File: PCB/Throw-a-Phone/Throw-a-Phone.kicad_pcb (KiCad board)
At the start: 2 copper layers, 50 x 87.5 mm, 26 parts, among them J3 Conn_01x04_Pin, SW1 SW_Push, SW10 SW_Push, SW11 SW_Push, SW12 SW_Push, SW2 SW_Push, SW3 SW_Push, SW4 SW_Push, SW5 SW_Push, SW6 SW_Push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

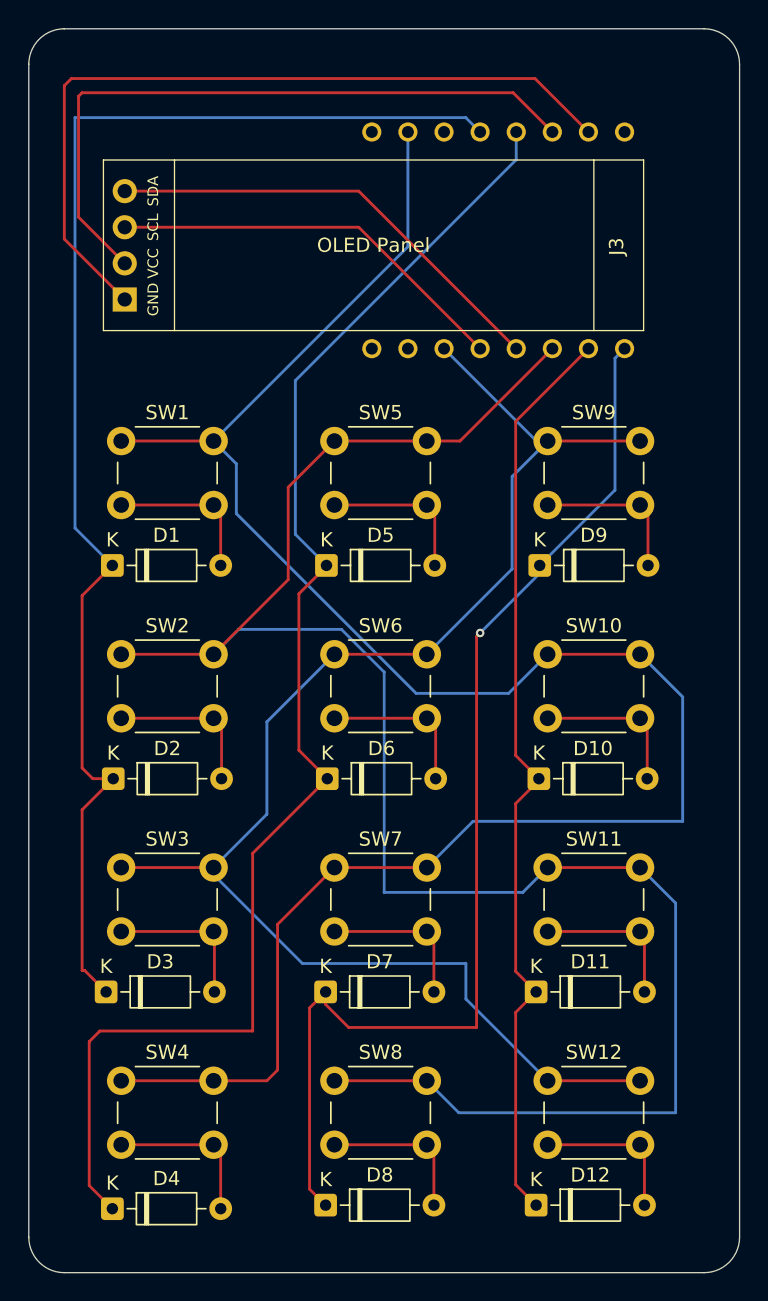
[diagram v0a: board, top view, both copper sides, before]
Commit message: Made enclosure, edited PCB
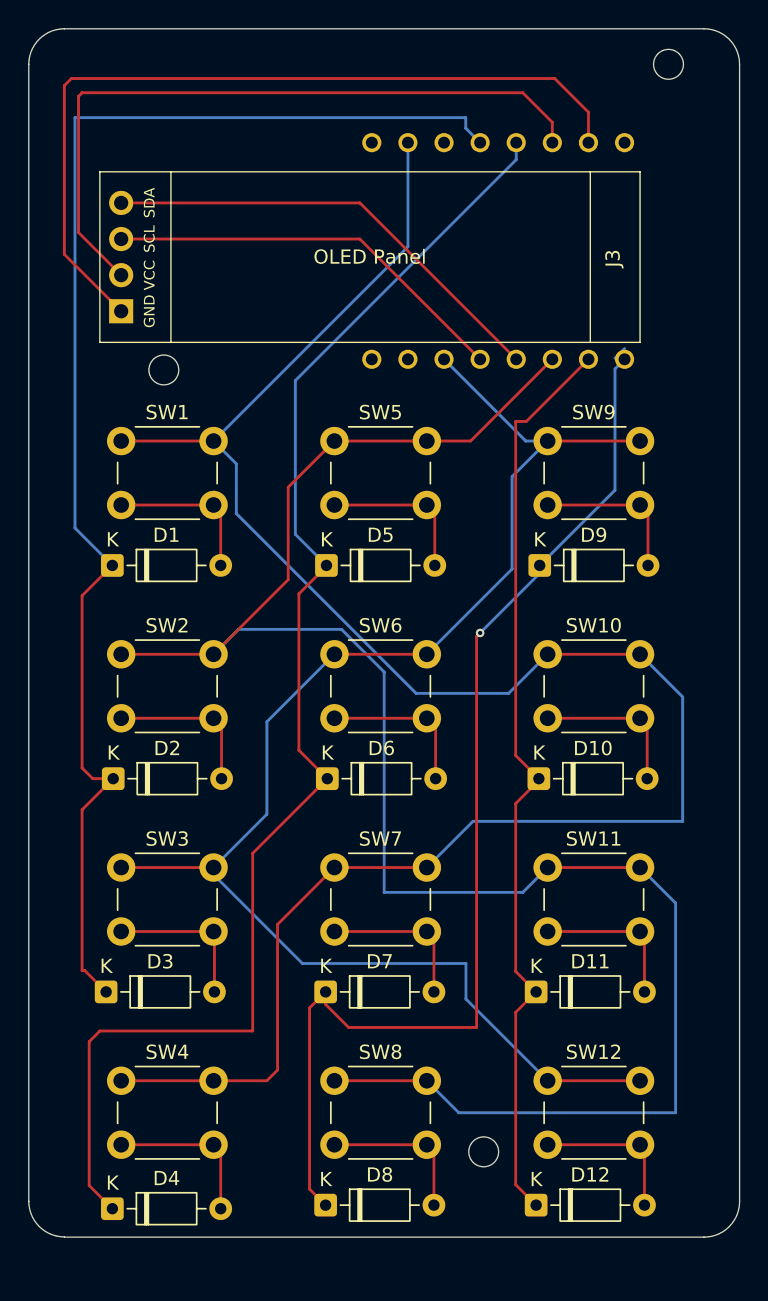
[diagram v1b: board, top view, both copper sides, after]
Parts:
- added REF**: MountingHole_2.1mm, MountingHole:MountingHole_2.1mm, F.Cu at (175.0, 57.5)
- added REF**: MountingHole_2.1mm, MountingHole:MountingHole_2.1mm, F.Cu at (162.0, 134.0)
- added REF**: MountingHole_2.1mm, MountingHole:MountingHole_2.1mm, F.Cu at (139.5, 79.0)
- moved J3 0.87 mm to (173.0, 77.1)
- moved U1 0.75 mm to (162.0, 70.6)
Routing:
- net GND: track 55.4 -> 57.7 mm
- net +3V3: track 47.7 -> 49.5 mm
- net ROW1: track 98.6 -> 97.9 mm
- net ROW0: track 95.9 -> 96.6 mm
- net COL0: track 140.5 -> 139.8 mm
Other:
- board size 50 x 87.5 mm -> 50 x 85 mm

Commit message: Updated readme, added images. Fixed PCB edge cuts
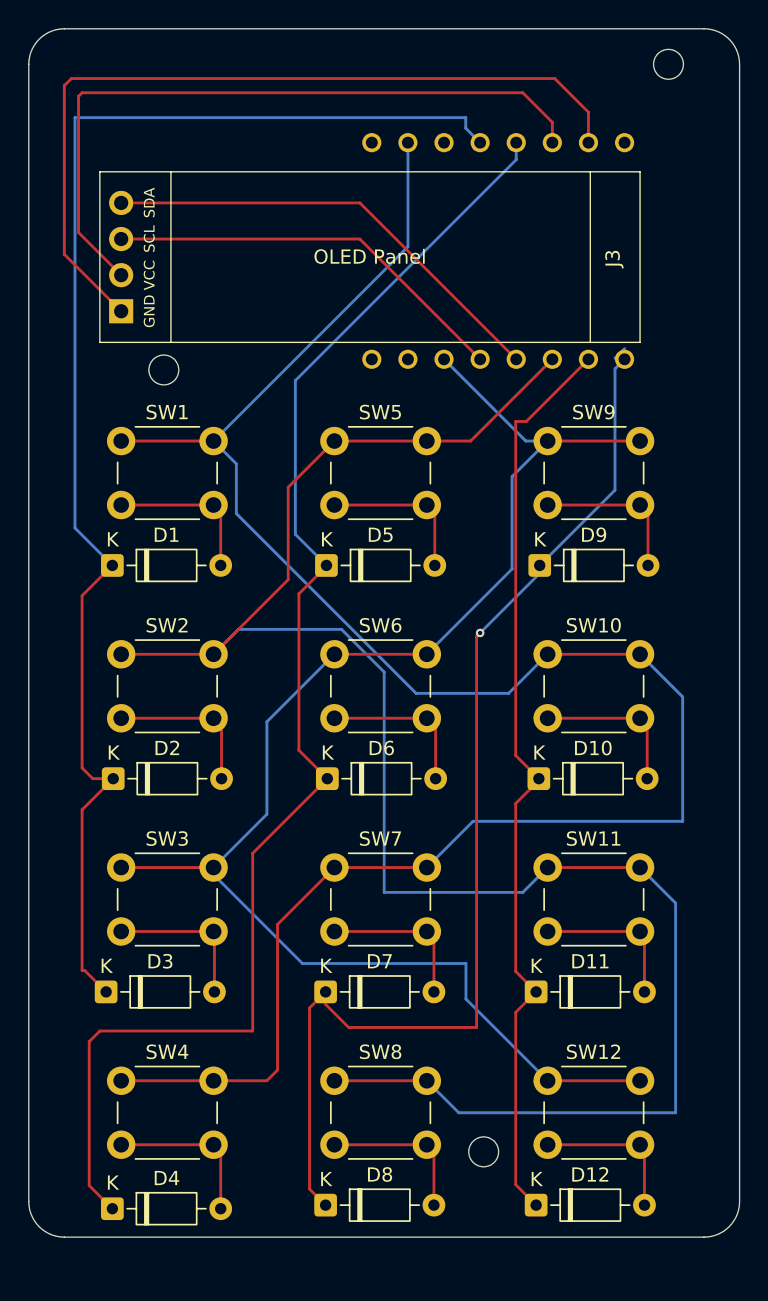
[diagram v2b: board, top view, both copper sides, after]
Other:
- board text added: "SDA"
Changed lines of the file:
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@@
-			)
-		)
-		(fp_text user "SDA"
-			(at 34.5 9.81 90)
-			(layer "F.SilkS")
-			(effects
-				(font
-					(size 0.75 0.75)
-					(thickness 0.15)
-				)
 			)
 		)
@@
 		(embedded_fonts no)
 	)
-	(gr_line
+	(gr_arc
 		(start 132.5 140)
-		(end 177.5 140)
+		(mid 130.732233 139.267767)
+		(end 130 137.5)
 		(stroke
 			(width 0.05)
@@
 		(layer "Edge.Cuts")
 	)
-	(gr_line
-		(start 177.5 55)
-		(end 132.5 55)
-		(stroke
-			(width 0.05)
-			(type default)
-		)
-		(layer "Edge.Cuts")
-	)
-	(gr_line
-		(start 130 57.5)
-		(end 130 137.5)
-		(stroke
-			(width 0.05)
-			(type default)
-		)
-		(layer "Edge.Cuts")
-	)
 	(gr_arc
 		(start 180 137.5)
@@
 	)
 	(gr_line
-		(start 180 137.5)
-		(end 180 57.5)
+		(start 132.5 55)
+		(end 177.5 55)
+		(stroke
+			(width 0.05)
+			(type default)
+		)
+		(layer "Edge.Cuts")
+	)
+	(gr_line
+		(start 130 137.5)
+		(end 130 57.5)
 		(stroke
 			(width 0.05)
@@
 		(layer "Edge.Cuts")
 	)
-	(gr_arc
-		(start 132.5 139.982233)
-		(mid 130.732233 139.25)
-		(end 130 137.482233)
+	(gr_line
+		(start 177.5 140)
+		(end 132.5 140)
 		(stroke
 			(width 0.05)
@@
 		(layer "Edge.Cuts")
 	)
+	(gr_line
+		(start 180 57.5)
+		(end 180 137.5)
+		(stroke
+			(width 0.05)
+			(type default)
+		)
+		(layer "Edge.Cuts")
+	)
+	(gr_text "SDA"
+		(at 138.5 67.25 90)
+		(layer "F.SilkS")
+		(effects
+			(font
+				(size 0.75 0.75)
+				(thickness 0.15)
+			)
+		)
+	)
 	(segment

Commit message: Update PCB, readme. Create gerbers
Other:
- board text added: "Throw-a-Phone!"
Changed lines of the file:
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@@
 			(plot_on_all_layers_selection 0x00000000_00000000_00000000_00000000)
 			(disableapertmacros no)
-			(usegerberextensions no)
+			(usegerberextensions yes)
 			(usegerberattributes yes)
 			(usegerberadvancedattributes yes)
-			(creategerberjobfile yes)
+			(creategerberjobfile no)
 			(dashed_line_dash_ratio 12.000000)
 			(dashed_line_gap_ratio 3.000000)
@@
 			(outputformat 1)
 			(mirror no)
-			(drillshape 1)
+			(drillshape 0)
 			(scaleselection 1)
-			(outputdirectory "")
+			(outputdirectory "D:/My folder/PROJECTS/Throw-a-Phone/production/")
 		)
 	)
@@
 		(layer "Edge.Cuts")
 	)
+	(gr_text "Throw-a-Phone!\n\n"
+		(at 142.5 66.5 0)
+		(layer "F.SilkS")
+		(effects
+			(font
+				(size 1.5 1.2)
+				(thickness 0.1)
+			)
+			(justify bottom)
+		)
+	)
 	(gr_text "SDA"
